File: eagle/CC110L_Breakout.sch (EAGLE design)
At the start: 28 parts

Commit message: almost completed board
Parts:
- added LOGO1: OSHW-LOGOS, SparkFun-Aesthetics:OSHW-LOGOS
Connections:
- net GDO0: now also JP1.6; no longer JP1.7
- net GDO2: now also JP1.5; no longer JP1.6
- net MISO: now also JP1.4; no longer JP1.3
- net RF_CS: now also JP1.7; no longer JP1.5
- net SCK: now also JP1.3; no longer JP1.4
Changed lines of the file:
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@@
 <part name="P+1" library="anoven" deviceset="VCC" device=""/>
 <part name="U$1" library="anoven" deviceset="GND" device=""/>
+<part name="LOGO1" library="SparkFun-Aesthetics" deviceset="OSHW-LOGO" device="S"/>
 </parts>
 <sheets>
@@
 <instance part="P+1" gate="VCC" x="198.12" y="127"/>
 <instance part="U$1" gate="GND" x="198.12" y="99.06"/>
+<instance part="LOGO1" gate="G$1" x="35.56" y="127"/>
 </instances>
 <busses>
@@
 </segment>
 <segment>
-<pinref part="JP1" gate="G$1" pin="3"/>
-<wire x1="205.74" y1="119.38" x2="198.12" y2="119.38" width="0.1524" layer="91"/>
-<label x="198.12" y="119.38" size="1.778" layer="95"/>
+<wire x1="205.74" y1="116.84" x2="198.12" y2="116.84" width="0.1524" layer="91"/>
+<label x="198.12" y="116.84" size="1.778" layer="95"/>
+<pinref part="JP1" gate="G$1" pin="4"/>
 </segment>
 </net>
@@
 </segment>
 <segment>
-<pinref part="JP1" gate="G$1" pin="4"/>
-<wire x1="205.74" y1="116.84" x2="198.12" y2="116.84" width="0.1524" layer="91"/>
-<label x="198.12" y="116.84" size="1.778" layer="95"/>
+<wire x1="205.74" y1="119.38" x2="198.12" y2="119.38" width="0.1524" layer="91"/>
+<label x="198.12" y="119.38" size="1.778" layer="95"/>
+<pinref part="JP1" gate="G$1" pin="3"/>
 </segment>
 </net>
@@
 </segment>
 <segment>
-<pinref part="JP1" gate="G$1" pin="5"/>
-<wire x1="205.74" y1="114.3" x2="198.12" y2="114.3" width="0.1524" layer="91"/>
-<label x="198.12" y="114.3" size="1.778" layer="95"/>
+<wire x1="205.74" y1="109.22" x2="198.12" y2="109.22" width="0.1524" layer="91"/>
+<pinref part="JP1" gate="G$1" pin="7"/>
+<label x="198.12" y="109.22" size="1.778" layer="95"/>
 </segment>
 </net>
 <net name="GDO2" class="0">
-<segment>
-<pinref part="JP1" gate="G$1" pin="6"/>
-<wire x1="205.74" y1="111.76" x2="198.12" y2="111.76" width="0.1524" layer="91"/>
-<label x="198.12" y="111.76" size="1.778" layer="95"/>
-</segment>
 <segment>
 <pinref part="U$10" gate="G$1" pin="GDO2"/>
 <wire x1="121.92" y1="66.04" x2="132.08" y2="66.04" width="0.1524" layer="91"/>
 </segment>
+<segment>
+<wire x1="205.74" y1="114.3" x2="198.12" y2="114.3" width="0.1524" layer="91"/>
+<pinref part="JP1" gate="G$1" pin="5"/>
+<label x="198.12" y="114.3" size="1.778" layer="95"/>
+</segment>
 </net>
 <net name="GDO0" class="0">
-<segment>
-<pinref part="JP1" gate="G$1" pin="7"/>
-<wire x1="205.74" y1="109.22" x2="198.12" y2="109.22" width="0.1524" layer="91"/>
-<label x="198.12" y="109.22" size="1.778" layer="95"/>
-</segment>
 <segment>
 <pinref part="U$10" gate="G$1" pin="GDO0"/>
 <wire x1="121.92" y1="48.26" x2="132.08" y2="48.26" width="0.1524" layer="91"/>
 </segment>
-</net>
+<segment>
+<wire x1="205.74" y1="111.76" x2="198.12" y2="111.76" width="0.1524" layer="91"/>
+<pinref part="JP1" gate="G$1" pin="6"/>
+<label x="198.12" y="111.76" size="1.778" layer="95"/>
+</segment>
+</net>

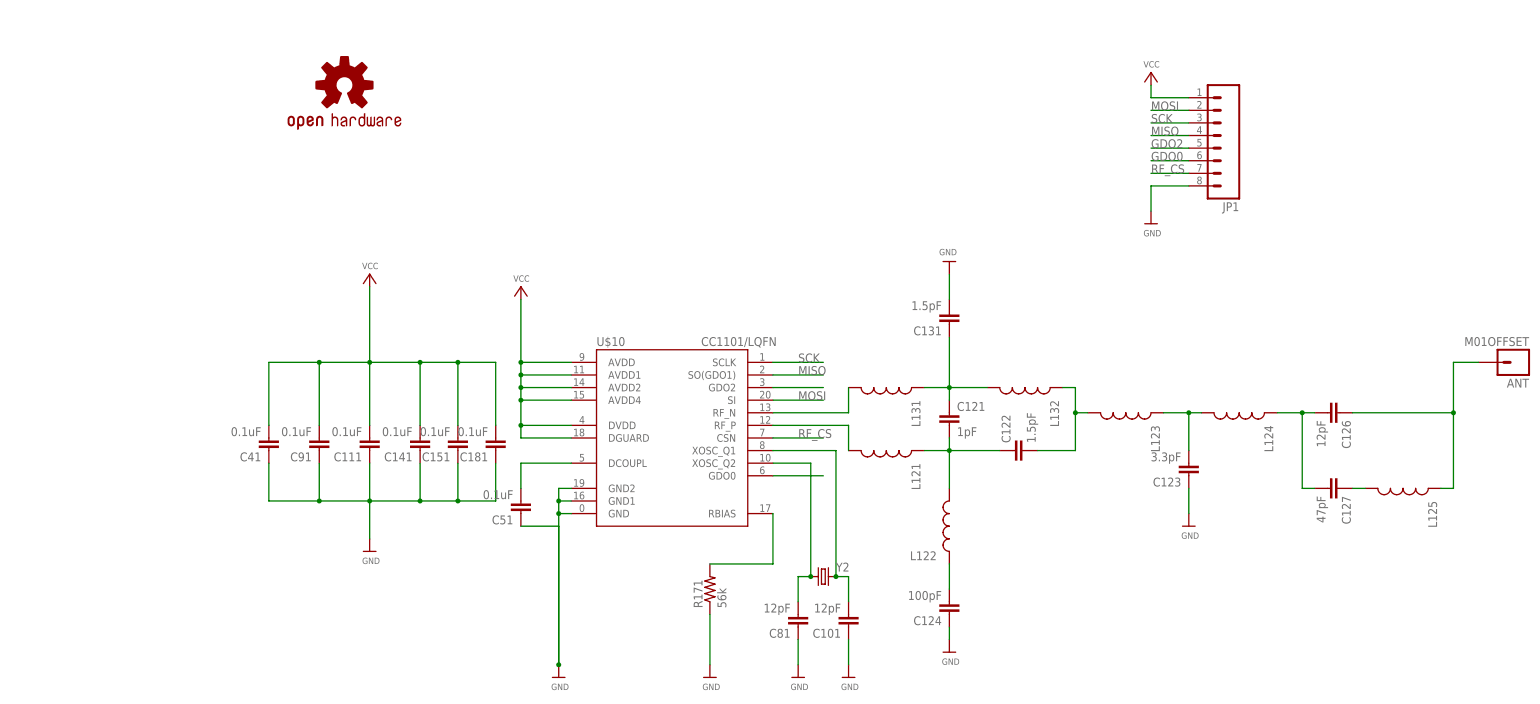
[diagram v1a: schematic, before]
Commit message: Finilized and uploaded to OSHpark ordered
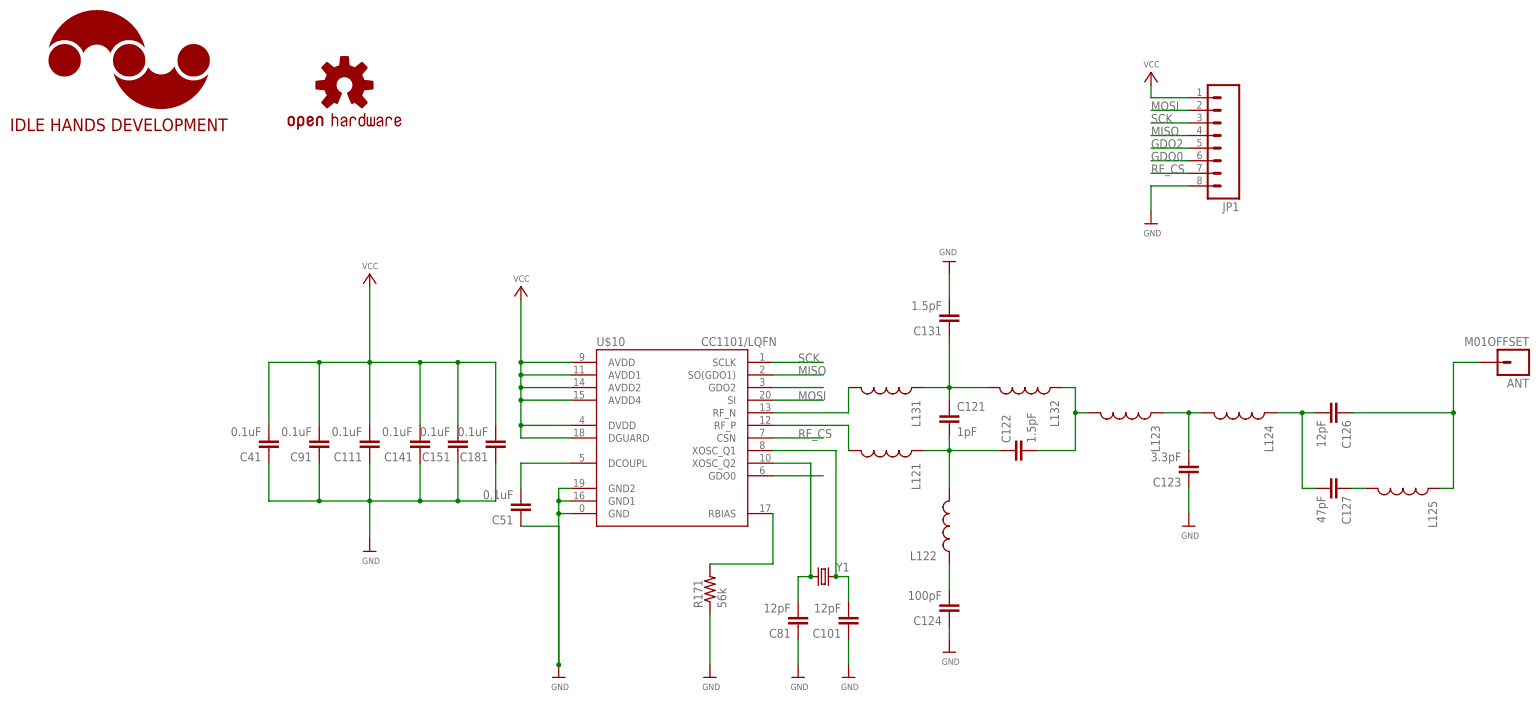
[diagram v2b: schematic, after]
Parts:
- added LOGO2: IDLEHANDS_LOGOS, IdleHandsProject:IDLEHANDS_LOGOS
- renumbered Y2 to Y1
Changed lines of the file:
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@@
 <?xml version="1.0" encoding="utf-8"?>
 <!DOCTYPE eagle SYSTEM "eagle.dtd">
-<eagle version="6.5.0">
+<eagle version="7.1.0">
 <drawing>
 <settings>
@@
 <grid distance="0.1" unitdist="inch" unit="inch" style="lines" multiple="1" display="no" altdistance="0.01" altunitdist="inch" altunit="inch"/>
 <layers>
-<layer number="1" name="Top" color="4" fill="1" visible="no" active="no"/>
-<layer number="2" name="Route2" color="1" fill="3" visible="no" active="no"/>
-<layer number="3" name="Route3" color="4" fill="3" visible="no" active="no"/>
-<layer number="14" name="Route14" color="1" fill="6" visible="no" active="no"/>
-<layer number="15" name="Route15" color="4" fill="6" visible="no" active="no"/>
-<layer number="16" name="Bottom" color="1" fill="1" visible="no" active="no"/>
-<layer number="17" name="Pads" color="2" fill="1" visible="no" active="no"/>
-<layer number="18" name="Vias" color="2" fill="1" visible="no" active="no"/>
-<layer number="19" name="Unrouted" color="6" fill="1" visible="no" active="no"/>
-<layer number="20" name="Dimension" color="15" fill="1" visible="no" active="no"/>
-<layer number="21" name="tPlace" color="7" fill="1" visible="no" active="no"/>
-<layer number="22" name="bPlace" color="7" fill="1" visible="no" active="no"/>
-<layer number="23" name="tOrigins" color="15" fill="1" visible="no" active="no"/>
-<layer number="24" name="bOrigins" color="15" fill="1" visible="no" active="no"/>
-<layer number="25" name="tNames" color="7" fill="1" visible="no" active="no"/>
-<layer number="26" name="bNames" color="7" fill="1" visible="no" active="no"/>
-<layer number="27" name="tValues" color="7" fill="1" visible="no" active="no"/>
-<layer number="28" name="bValues" color="7" fill="1" visible="no" active="no"/>
+<layer number="1" name="Top" color="4" fill="1" visible="yes" active="no"/>
+<layer number="2" name="Route2" color="1" fill="3" visible="yes" active="no"/>
+<layer number="3" name="Route3" color="4" fill="3" visible="yes" active="no"/>
+<layer number="14" name="Route14" color="1" fill="6" visible="yes" active="no"/>
+<layer number="15" name="Route15" color="4" fill="6" visible="yes" active="no"/>
+<layer number="16" name="Bottom" color="1" fill="1" visible="yes" active="no"/>
+<layer number="17" name="Pads" color="2" fill="1" visible="yes" active="no"/>
+<layer number="18" name="Vias" color="2" fill="1" visible="yes" active="no"/>
+<layer number="19" name="Unrouted" color="6" fill="1" visible="yes" active="no"/>
+<layer number="20" name="Dimension" color="15" fill="1" visible="yes" active="no"/>
+<layer number="21" name="tPlace" color="7" fill="1" visible="yes" active="no"/>
+<layer number="22" name="bPlace" color="7" fill="1" visible="yes" active="no"/>
+<layer number="23" name="tOrigins" color="15" fill="1" visible="yes" active="no"/>
+<layer number="24" name="bOrigins" color="15" fill="1" visible="yes" active="no"/>
+<layer number="25" name="tNames" color="7" fill="1" visible="yes" active="no"/>
+<layer number="26" name="bNames" color="7" fill="1" visible="yes" active="no"/>
+<layer number="27" name="tValues" color="7" fill="1" visible="yes" active="no"/>
+<layer number="28" name="bValues" color="7" fill="1" visible="yes" active="no"/>
 <layer number="29" name="tStop" color="7" fill="3" visible="no" active="no"/>
 <layer number="30" name="bStop" color="7" fill="6" visible="no" active="no"/>
@@
 <layer number="35" name="tGlue" color="7" fill="4" visible="no" active="no"/>
 <layer number="36" name="bGlue" color="7" fill="5" visible="no" active="no"/>
-<layer number="37" name="tTest" color="7" fill="1" visible="no" active="no"/>
-<layer number="38" name="bTest" color="7" fill="1" visible="no" active="no"/>
+<layer number="37" name="tTest" color="7" fill="1" visible="yes" active="no"/>
+<layer number="38" name="bTest" color="7" fill="1" visible="yes" active="no"/>
 <layer number="39" name="tKeepout" color="4" fill="11" visible="no" active="no"/>
 <layer number="40" name="bKeepout" color="1" fill="11" visible="no" active="no"/>
@@
 <layer number="44" name="Drills" color="7" fill="1" visible="no" active="no"/>
 <layer number="45" name="Holes" color="7" fill="1" visible="no" active="no"/>
-<layer number="46" name="Milling" color="3" fill="1" visible="no" active="no"/>
-<layer number="47" name="Measures" color="7" fill="1" visible="no" active="no"/>
-<layer number="48" name="Document" color="7" fill="1" visible="no" active="no"/>
-<layer number="49" name="Reference" color="7" fill="1" visible="no" active="no"/>
-<layer number="50" name="dxf" color="7" fill="1" visible="no" active="no"/>
-<layer number="51" name="tDocu" color="7" fill="1" visible="no" active="no"/>
-<layer number="52" name="bDocu" color="7" fill="1" visible="no" active="no"/>
-<layer number="53" name="tGND_GNDA" color="7" fill="9" visible="no" active="no"/>
-<layer number="54" name="bGND_GNDA" color="1" fill="9" visible="no" active="no"/>
-<layer number="56" name="wert" color="7" fill="1" visible="no" active="no"/>
+<layer number="46" name="Milling" color="3" fill="1" visible="yes" active="no"/>
+<layer number="47" name="Measures" color="7" fill="1" visible="yes" active="no"/>
+<layer number="48" name="Document" color="7" fill="1" visible="yes" active="no"/>
+<layer number="49" name="Reference" color="7" fill="1" visible="yes" active="no"/>
+<layer number="50" name="dxf" color="7" fill="1" visible="yes" active="no"/>
+<layer number="51" name="tDocu" color="7" fill="1" visible="yes" active="no"/>
+<layer number="52" name="bDocu" color="7" fill="1" visible="yes" active="no"/>
+<layer number="53" name="tGND_GNDA" color="7" fill="9" visible="yes" active="no"/>
+<layer number="54" name="bGND_GNDA" color="1" fill="9" visible="yes" active="no"/>
+<layer number="56" name="wert" color="7" fill="1" visible="yes" active="no"/>
 <layer number="91" name="Nets" color="2" fill="1" visible="yes" active="yes"/>
 <layer number="92" name="Busses" color="1" fill="1" visible="yes" active="yes"/>
@@
 <part name="C127" library="rcl" deviceset="C-EU" device="C0402" value="47pF"/>
 <part name="L125" library="SparkFun-Passives" deviceset="INDUCTOR" device="0402"/>
-<part name="Y2" library="SparkFun-FreqCtrl" deviceset="CRYSTAL" device="" technology="3.2X2.5"/>
+<part name="Y1" library="SparkFun-FreqCtrl" deviceset="CRYSTAL" device="" technology="3.2X2.5"/>
 <part name="C81" library="rcl" deviceset="C-EU" device="C0402" value="12pF"/>
 <part name="C101" library="rcl" deviceset="C-EU" device="C0402" value="12pF"/>
@@
 <part name="U$1" library="anoven" deviceset="GND" device=""/>
 <part name="LOGO1" library="SparkFun-Aesthetics" deviceset="OSHW-LOGO" device="S"/>
+<part name="LOGO2" library="IdleHandsProject" deviceset="IDLEHANDS_LOGO" device="S" value="IDLEHANDS_LOGOS"/>
 </parts>
 <sheets>
@@
 <instance part="C127" gate="G$1" x="236.22" y="45.72" rot="R270"/>
 <instance part="L125" gate="G$1" x="248.92" y="45.72" rot="R270"/>
-<instance part="Y2" gate="G$1" x="132.08" y="27.94"/>
+<instance part="Y1" gate="G$1" x="132.08" y="27.94"/>
 <instance part="C81" gate="G$1" x="127" y="17.78" rot="R180"/>
 <instance part="C101" gate="G$1" x="137.16" y="17.78" rot="R180"/>
@@
 <instance part="U$1" gate="GND" x="198.12" y="99.06"/>
 <instance part="LOGO1" gate="G$1" x="35.56" y="127"/>
+<instance part="LOGO2" gate="G$1" x="-7.62" y="132.08"/>
 </instances>
 <busses>
@@
 <segment>
 <pinref part="U$10" gate="G$1" pin="XOSC_Q1"/>
-<pinref part="Y2" gate="G$1" pin="2"/>
+<pinref part="Y1" gate="G$1" pin="2"/>
 <wire x1="121.92" y1="53.34" x2="134.62" y2="53.34" width="0.1524" layer="91"/>
 <wire x1="134.62" y1="53.34" x2="134.62" y2="27.94" width="0.1524" layer="91"/>
@@
 <segment>
 <pinref part="U$10" gate="G$1" pin="XOSC_Q2"/>
-<pinref part="Y2" gate="G$1" pin="1"/>
+<pinref part="Y1" gate="G$1" pin="1"/>
 <wire x1="121.92" y1="50.8" x2="129.54" y2="50.8" width="0.1524" layer="91"/>
 <wire x1="129.54" y1="50.8" x2="129.54" y2="27.94" width="0.1524" layer="91"/>
